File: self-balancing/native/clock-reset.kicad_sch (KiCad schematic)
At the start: 9 parts, among them U12 TLV803EA29DBZR, X1 8MHz / CL12pF

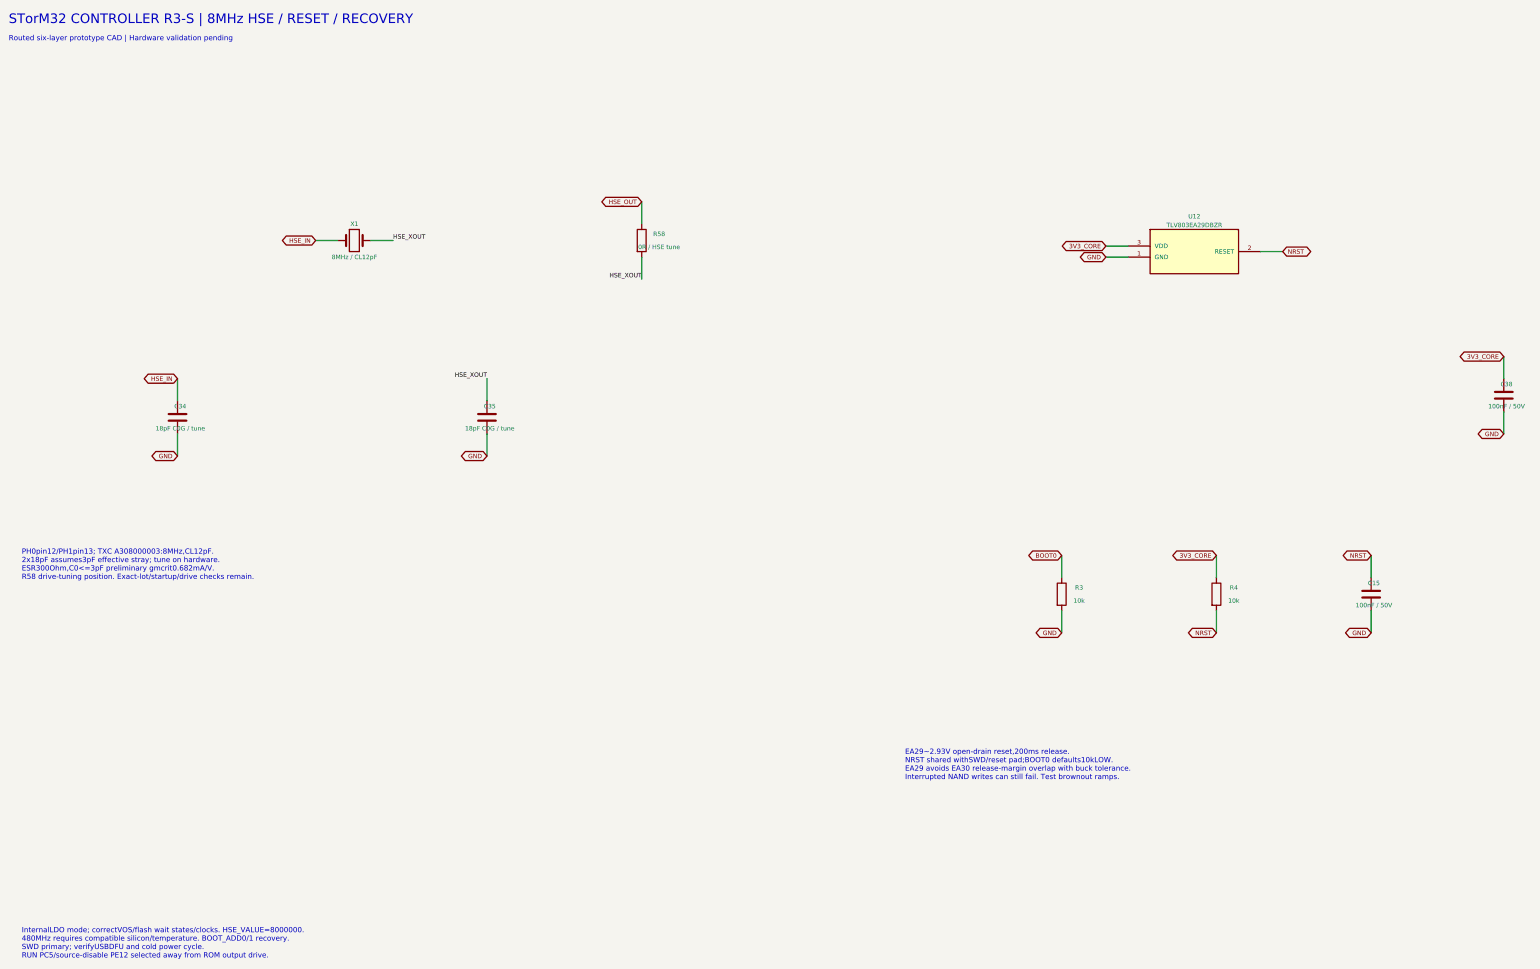
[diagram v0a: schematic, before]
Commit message: Improve H743 schematic readability with wired functional groups
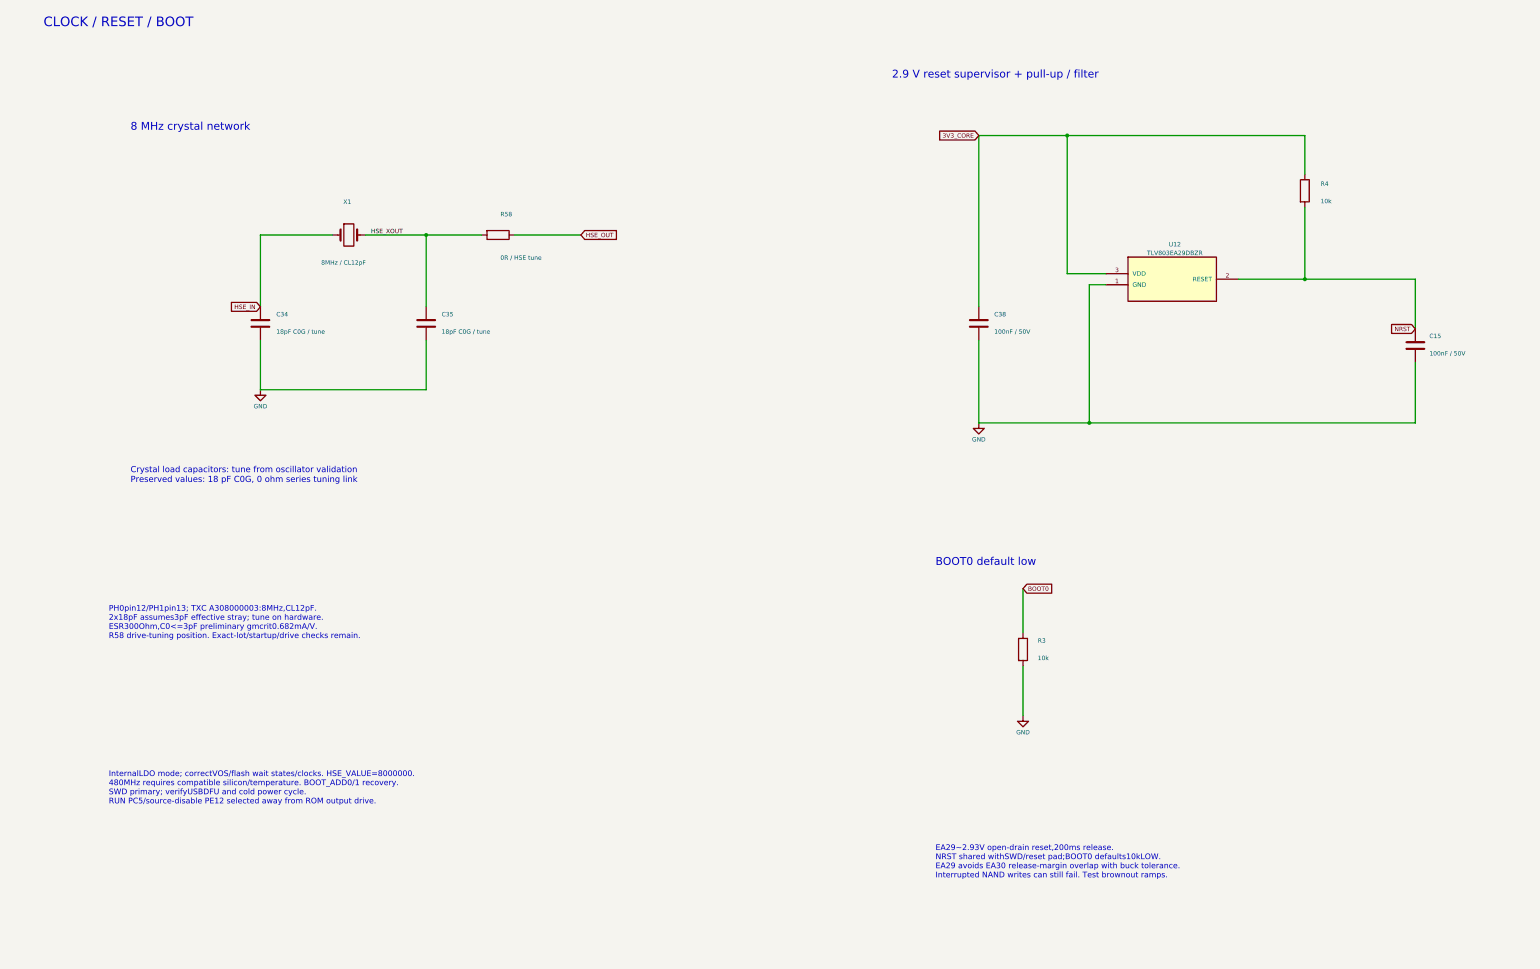
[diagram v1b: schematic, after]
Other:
- note added: "2.9 V reset supervisor + pull-up / filter"
- note added: "8 MHz crystal network"
- note added: "BOOT0 default low"
- note added: "CLOCK / RESET / BOOT"
- note added: "Crystal load capacitors: tune from oscillator validation Preserved values: 18 pF C0G, 0 ohm series tuning link"
- note removed: "Routed six-layer prototype CAD | Hardware validation pending"
- note removed: "STorM32 CONTROLLER R3-S | 8MHz HSE / RESET / RECOVERY"
- moved on the sheet: C15, C34, C35, C38, R3, R4, R58, U12, X1
